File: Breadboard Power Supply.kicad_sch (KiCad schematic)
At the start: 17 parts, among them J1 Conn_01x02_Pin, J2 Conn_01x02_Pin, J3 Conn_01x03_Pin, J4 Conn_01x03_Pin, J5 Screw_Terminal_01x02, J6 Screw_Terminal_01x02, J7 Barrel_Jack_Switch, SW1 SW_Wuerth_450301014042, U1 LM7805_TO220, U2 LM317_TO-220

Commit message: Update schematic
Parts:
- D1: Purpose (none) -> Power input indicator
- J1, J2: Purpose (none) -> Output to breadboard
- J3: Purpose (none) -> Output Voltage Selector 1
- J4: Purpose (none) -> Output Voltage Selector 2
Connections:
- net PWR_output: now reaches J1.2 (Pin_2), J4.2 (Pin_2), J5.2 (Pin_2)
- net PWR_output: now also J2.2 (Pin_2), J3.2 (Pin_2), J6.2 (Pin_2)
- net PWR_input: now reaches J7.1, SW1.1 (B)
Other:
- note added: "3.3V Circuit"
- note added: "Input & 5V circuit"
- note added: "Output & Switches"
- note added: "screw terminals flipped vertically so pin 1 becomes ground (and stays below pin 2)"
- moved on the sheet: C1, C2, C3, D1, J1, J2, J3, J4, J5, J6, J7, R1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

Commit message: Update PCB Design
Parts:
- removed J3, J4: Conn_01x03_Pin, Connector_PinHeader_2.54mm:PinHeader_1x03_P2.54mm_Vertical, symbol Connector:Conn_01x03_Pin
- added S1, S2: EG1218, EG1218 SPDT Switch:SW_EG1218, symbol EG1218:EG1218
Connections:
- net 3.3V: now also S1.3, S2.3
- net 5V: now also S1.1, S2.1
- net PWR_output: now also S1.2, S2.2

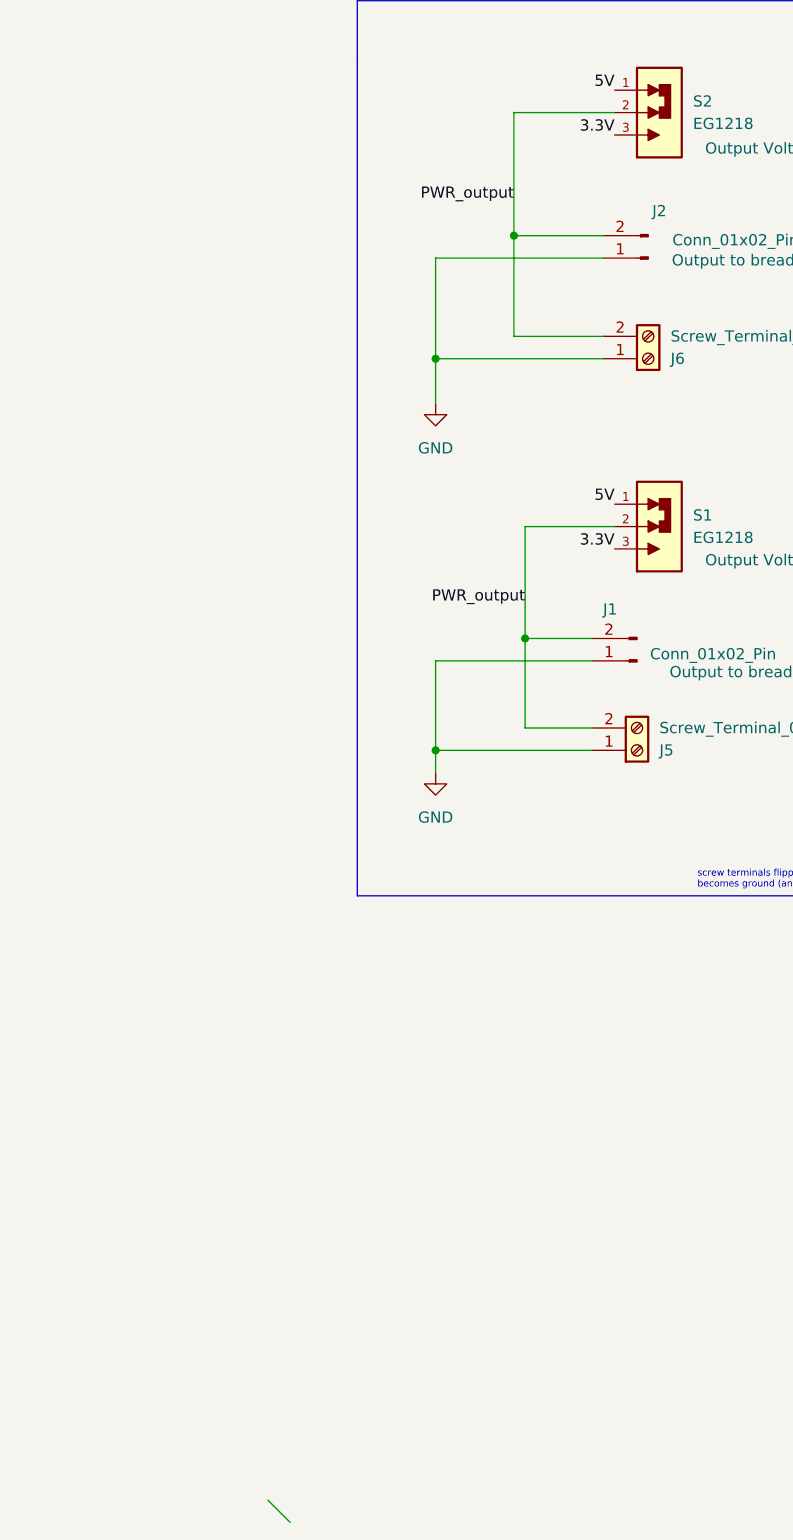
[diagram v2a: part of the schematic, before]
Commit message: Fix bug in schematic
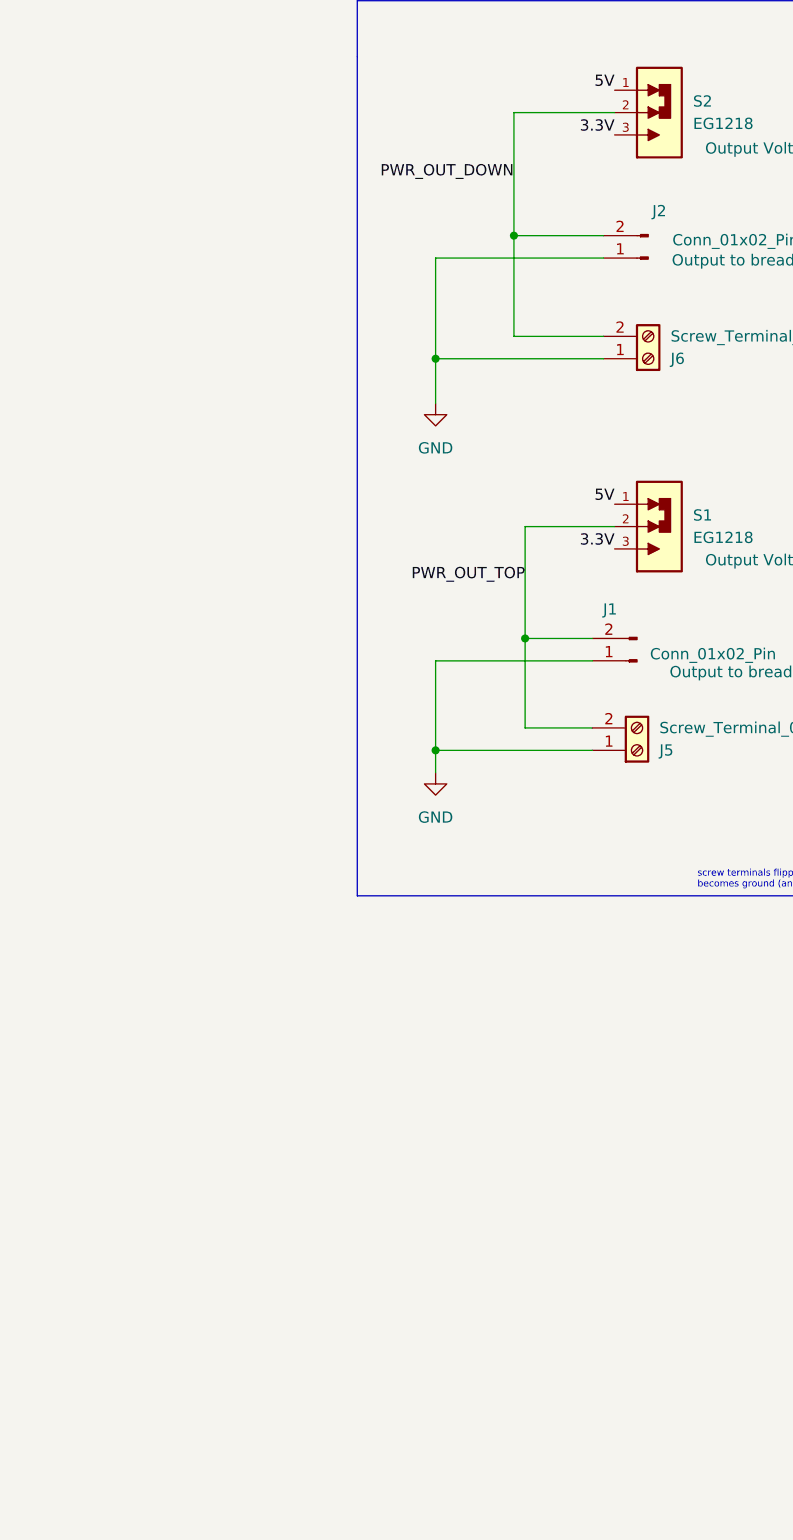
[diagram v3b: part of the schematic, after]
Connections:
- net PWR_output renamed PWR_OUT_DOWN
- net PWR_OUT_DOWN: no longer J1.2 (Pin_2), J5.2 (Pin_2), S1.2
- new net PWR_OUT_TOP: J1.2 (Pin_2), J5.2 (Pin_2), S1.2
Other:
- title: KiCad Practice Design with Breadboard Power Supply -> Breadboard Power Supply Design
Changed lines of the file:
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@@
 	(paper "A4")
 	(title_block
-		(title "KiCad Practice Design with Breadboard Power Supply")
+		(title "Breadboard Power Supply Design")
 		(date "2025-09-23")
-		(rev "1.0")
+		(rev "2.0")
 		(company "Henry Munachimso")
 	)
@@
 		(at 81.28 53.34)
 	)
-	(bus_entry
-		(at 190.5 214.63)
-		(size 2.54 2.54)
-		(stroke
-			(width 0)
-			(type default)
-		)
-	)
 	(wire
 		(pts
@@
 		)
 	)
-	(label "PWR_output"
-		(at 219.71 113.03 180)
-		(effects
-			(font
-				(size 1.27 1.27)
-			)
-			(justify right bottom)
-		)
-	)
 	(label "12V"
 		(at 87.63 48.26 0)
@@
 		)
 	)
-	(label "PWR_output"
-		(at 218.44 67.31 180)
-		(effects
-			(font
-				(size 1.27 1.27)
-			)
-			(justify right bottom)
-		)
-	)
 	(label "5V"
 		(at 229.87 54.61 180)
 		(effects
 			(font
+				(size 1.27 1.27)
+			)
+			(justify right bottom)
+		)
+	)
+	(label "PWR_OUT_TOP"
+		(at 219.71 110.49 180)
+		(effects
+			(font
+				(size 1.27 1.27)
+			)
+			(justify right bottom)
+		)
+	)
+	(label "PWR_OUT_DOWN"
+		(at 218.44 64.77 180)
+		(effects
+			(font
